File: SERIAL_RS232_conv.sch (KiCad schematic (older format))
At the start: 9 parts

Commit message: .bak ignore rule
Ignore bak files
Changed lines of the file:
@@
 $EndComp
 Wire Wire Line
-	2250 3550 2200 3550
-Wire Wire Line
-	2200 3550 2150 3550
+	2150 3550 2250 3550
 Wire Wire Line
 	1850 3550 1750 3550
 Wire Wire Line
-	1750 3350 1750 3550
+	1750 3350 1750 3750
 Wire Wire Line
-	1750 3550 1750 3750
-Wire Wire Line
-	1700 3750 1750 3750
-Wire Wire Line
-	1750 3750 2250 3750
+	1700 3750 2250 3750
 Wire Wire Line
 	2250 3950 2150 3950
@@
 	3650 3450 3700 3450
 Wire Wire Line
-	3700 3450 3700 3550
-Wire Wire Line
-	3700 3550 3700 3650
+	3700 3450 3700 3650
 Wire Wire Line
 	3700 3550 3750 3550
@@
 $EndComp
 Wire Wire Line
-	2200 3300 2200 3350
-Wire Wire Line
-	2200 3350 2200 3550
+	2200 3300 2200 3550
 Connection ~ 2200 3550
 Wire Wire Line

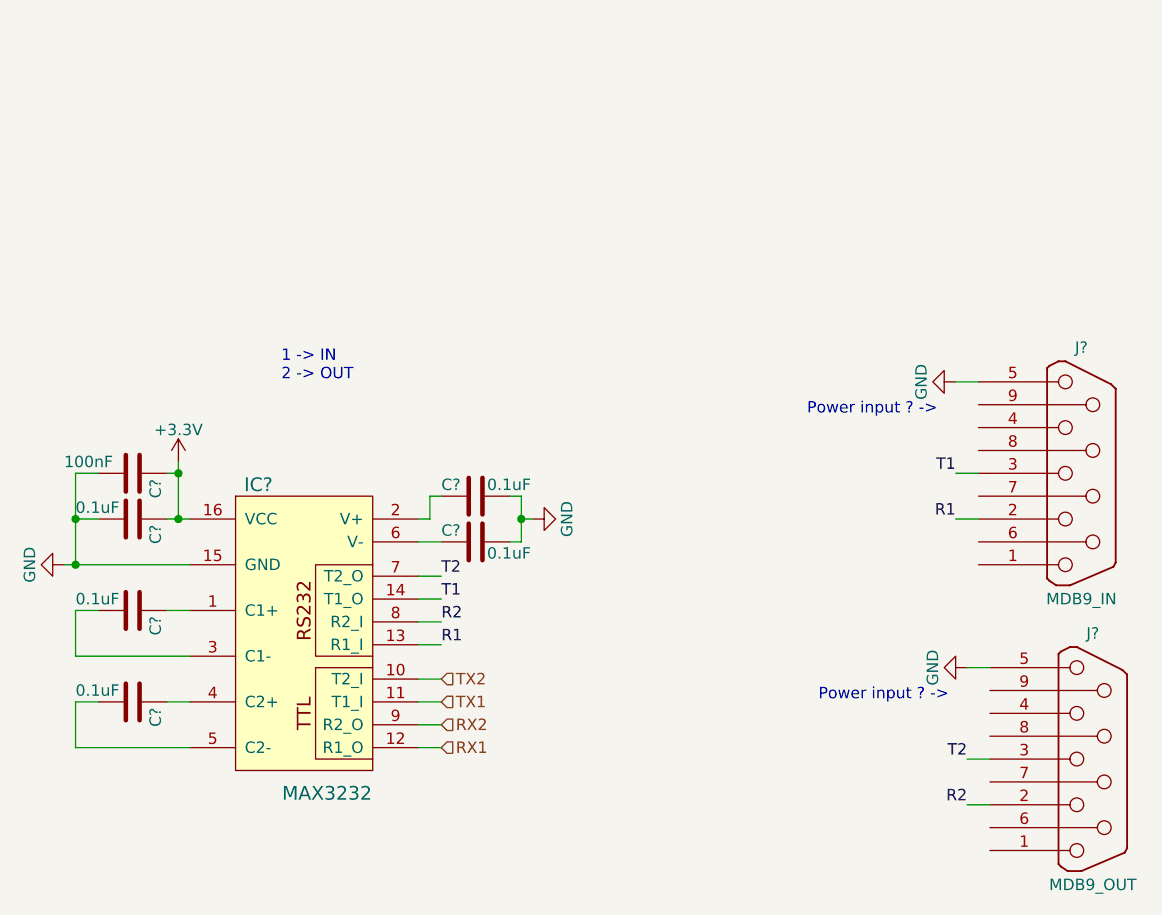
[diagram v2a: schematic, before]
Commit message: Schematic correction
Corrected the direction on some signals. Added a pin header for general development.
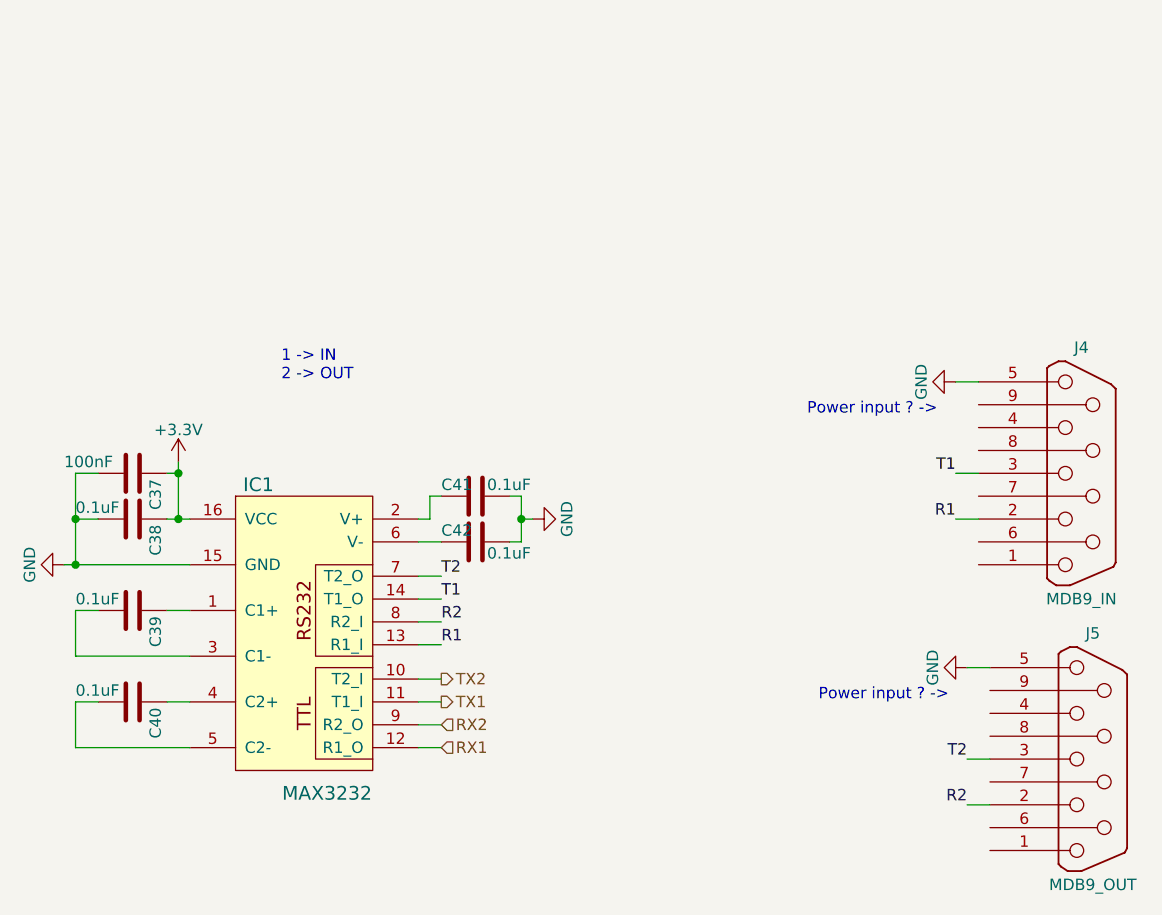
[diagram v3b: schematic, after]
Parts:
- C37, C38, C39, C40, C41, C42: renamed from C?; footprint (none) -> Capacitors_SMD:C_0603_HandSoldering
- gave numbers to parts that had none: 3
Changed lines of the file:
@@
 $EndDescr
 $Comp
-L MAX3232 IC?
+L MAX3232 IC1
 U 1 1 588F1DDD
 P 2750 3850
-F 0 "IC?" H 2550 4300 60  0000 C CNN
+F 0 "IC1" H 2550 4300 60  0000 C CNN
 F 1 "MAX3232" H 2850 2950 60  0000 C CNN
-F 2 "" H 2750 3850 60  0000 C CNN
+F 2 "" H 2750 3850 60  0001 C CNN
 F 3 "" H 2750 3850 60  0000 C CNN
 	1    2750 3850
@@
 $EndComp
 $Comp
-L DB9 J?
+L DB9 J4
 U 1 1 588F1EC2
 P 6150 3350
-F 0 "J?" H 6150 3900 50  0000 C CNN
+F 0 "J4" H 6150 3900 50  0000 C CNN
 F 1 "MDB9_IN" H 6150 2800 50  0000 C CNN
-F 2 "" H 6150 3350 50  0000 C CNN
+F 2 "" H 6150 3350 50  0001 C CNN
 F 3 "" H 6150 3350 50  0000 C CNN
 	1    6150 3350
@@
 $EndComp
 $Comp
-L DB9 J?
+L DB9 J5
 U 1 1 588F1F2B
 P 6200 4600
-F 0 "J?" H 6200 5150 50  0000 C CNN
+F 0 "J5" H 6200 5150 50  0000 C CNN
 F 1 "MDB9_OUT" H 6200 4050 50  0000 C CNN
-F 2 "" H 6200 4600 50  0000 C CNN
+F 2 "" H 6200 4600 50  0001 C CNN
 F 3 "" H 6200 4600 50  0000 C CNN
 	1    6200 4600
@@
 $EndComp
 $Comp
-L GND #PWR054
+L GND #PWR069
 U 1 1 588F1FE7
 P 5600 2950
-F 0 "#PWR054" H 5600 2700 50  0001 C CNN
+F 0 "#PWR069" H 5600 2700 50  0001 C CNN
 F 1 "GND" H 5600 2800 50  0000 C CNN
 F 2 "" H 5600 2950 50  0000 C CNN
@@
 $EndComp
 $Comp
-L GND #PWR055
+L GND #PWR070
 U 1 1 588F2002
 P 5650 4200
-F 0 "#PWR055" H 5650 3950 50  0001 C CNN
+F 0 "#PWR070" H 5650 3950 50  0001 C CNN
 F 1 "GND" H 5650 4050 50  0000 C CNN
 F 2 "" H 5650 4200 50  0000 C CNN
@@
 $EndComp
 $Comp
-L C C?
+L C C39
 U 1 1 588F207B
 P 2000 3950
-F 0 "C?" H 2025 4050 50  0000 L CNN
+F 0 "C39" H 2025 4050 50  0000 L CNN
 F 1 "0.1uF" V 1950 3700 50  0000 L CNN
-F 2 "" H 2038 3800 50  0000 C CNN
+F 2 "Capacitors_SMD:C_0603_HandSoldering" H 2038 3800 50  0001 C CNN
 F 3 "" H 2000 3950 50  0000 C CNN
 	1    2000 3950
@@
 $EndComp
 $Comp
-L C C?
+L C C40
 U 1 1 588F20EE
 P 2000 4350
-F 0 "C?" H 2025 4450 50  0000 L CNN
+F 0 "C40" H 2025 4450 50  0000 L CNN
 F 1 "0.1uF" V 1950 4100 50  0000 L CNN
-F 2 "" H 2038 4200 50  0000 C CNN
+F 2 "Capacitors_SMD:C_0603_HandSoldering" H 2038 4200 50  0001 C CNN
 F 3 "" H 2000 4350 50  0000 C CNN
 	1    2000 4350
@@
 $EndComp
 $Comp
-L C C?
+L C C38
 U 1 1 588F21DD
 P 2000 3550
-F 0 "C?" H 2025 3650 50  0000 L CNN
+F 0 "C38" H 2025 3650 50  0000 L CNN
 F 1 "0.1uF" V 1950 3300 50  0000 L CNN
-F 2 "" H 2038 3400 50  0000 C CNN
+F 2 "Capacitors_SMD:C_0603_HandSoldering" H 2038 3400 50  0001 C CNN
 F 3 "" H 2000 3550 50  0000 C CNN
 	1    2000 3550
@@
 	1750 4550 2250 4550
 $Comp
-L GND #PWR056
+L GND #PWR071
 U 1 1 588F251A
 P 3750 3550
-F 0 "#PWR056" H 3750 3300 50  0001 C CNN
+F 0 "#PWR071" H 3750 3300 50  0001 C CNN
 F 1 "GND" H 3750 3400 50  0000 C CNN
 F 2 "" H 3750 3550 50  0000 C CNN
@@
 Connection ~ 3700 3550
 $Comp
-L GND #PWR057
+L GND #PWR072
 U 1 1 588F266A
 P 1700 3750
-F 0 "#PWR057" H 1700 3500 50  0001 C CNN
+F 0 "#PWR072" H 1700 3500 50  0001 C CNN
 F 1 "GND" H 1700 3600 50  0000 C CNN
 F 2 "" H 1700 3750 50  0000 C CNN
@@
 Connection ~ 1750 3750
 $Comp
-L +3.3V #PWR058
+L +3.3V #PWR073
 U 1 1 588F26E1
 P 2200 3300
-F 0 "#PWR058" H 2200 3150 50  0001 C CNN
+F 0 "#PWR073" H 2200 3150 50  0001 C CNN
 F 1 "+3.3V" H 2200 3440 50  0000 C CNN
 F 2 "" H 2200 3300 50  0000 C CNN
@@
 $EndComp
 $Comp
-L C C?
+L C C37
 U 1 1 588F2970
 P 2000 3350
-F 0 "C?" H 2025 3450 50  0000 L CNN
+F 0 "C37" H 2025 3450 50  0000 L CNN
 F 1 "100nF" V 1950 3050 50  0000 L CNN
-F 2 "" H 2038 3200 50  0000 C CNN
+F 2 "Capacitors_SMD:C_0603_HandSoldering" H 2038 3200 50  0001 C CNN
 F 3 "" H 2000 3350 50  0000 C CNN
 	1    2000 3350
@@
 Connection ~ 1750 3550
 $Comp
-L C C?
+L C C41
 U 1 1 588F31D0
 P 3500 3450
-F 0 "C?" V 3450 3300 50  0000 L CNN
+F 0 "C41" V 3450 3300 50  0000 L CNN
 F 1 "0.1uF" V 3450 3500 50  0000 L CNN
-F 2 "" H 3538 3300 50  0000 C CNN
+F 2 "Capacitors_SMD:C_0603_HandSoldering" H 3538 3300 50  0001 C CNN
 F 3 "" H 3500 3450 50  0000 C CNN
 	1    3500 3450
@@
 $EndComp
 $Comp
-L C C?
+L C C42
 U 1 1 588F320C
 P 3500 3650
-F 0 "C?" V 3450 3500 50  0000 L CNN
+F 0 "C42" V 3450 3500 50  0000 L CNN
 F 1 "0.1uF" V 3550 3700 50  0000 L CNN
-F 2 "" H 3538 3500 50  0000 C CNN
+F 2 "Capacitors_SMD:C_0603_HandSoldering" H 3538 3500 50  0001 C CNN
 F 3 "" H 3500 3650 50  0000 C CNN
 	1    3500 3650
@@
 Wire Wire Line
 	5650 4200 5750 4200
-Text HLabel 3350 4350 2    50   Input ~ 0
+Text HLabel 3350 4350 2    50   Output ~ 0
 TX1
-Text HLabel 3350 4250 2    50   Input ~ 0
+Text HLabel 3350 4250 2    50   Output ~ 0
 TX2
 Text HLabel 3350 4450 2    50   Input ~ 0

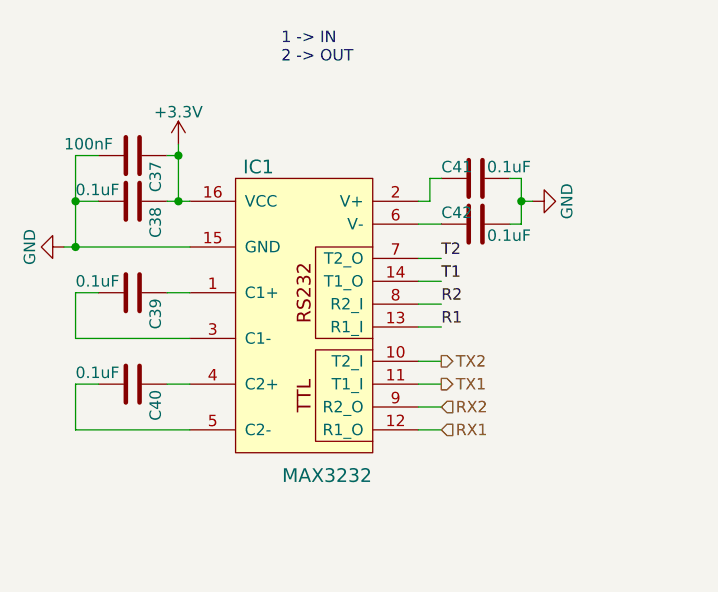
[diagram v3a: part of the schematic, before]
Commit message: Modified LAN9500A schematic.
Modified the schematic for the USB to Ethernet converter.
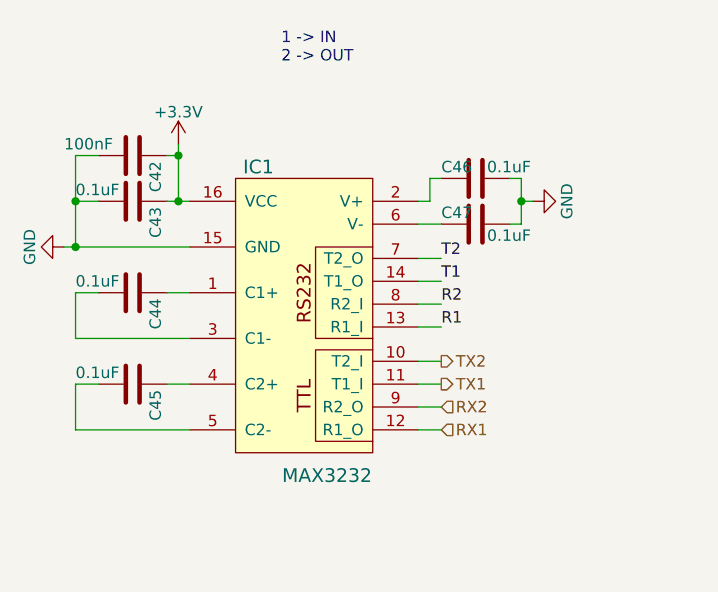
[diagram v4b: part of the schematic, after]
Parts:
- C42: renamed from C37; footprint Capacitors_SMD:C_0603_HandSoldering -> Capacitors_SMD:C_0805_HandSoldering
- C43: renamed from C38; footprint Capacitors_SMD:C_0603_HandSoldering -> Capacitors_SMD:C_0805_HandSoldering
- C44: renamed from C39; footprint Capacitors_SMD:C_0603_HandSoldering -> Capacitors_SMD:C_0805_HandSoldering
- C45: renamed from C40; footprint Capacitors_SMD:C_0603_HandSoldering -> Capacitors_SMD:C_0805_HandSoldering
- C46: renamed from C41; footprint Capacitors_SMD:C_0603_HandSoldering -> Capacitors_SMD:C_0805_HandSoldering
- C47: renamed from C42; footprint Capacitors_SMD:C_0603_HandSoldering -> Capacitors_SMD:C_0805_HandSoldering
- J4, J5: footprint (none) -> Connectors:DB9FC
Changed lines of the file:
@@
 F 0 "J4" H 6150 3900 50  0000 C CNN
 F 1 "MDB9_IN" H 6150 2800 50  0000 C CNN
-F 2 "" H 6150 3350 50  0001 C CNN
+F 2 "Connectors:DB9FC" H 6150 3350 50  0001 C CNN
 F 3 "" H 6150 3350 50  0000 C CNN
 	1    6150 3350
@@
 F 0 "J5" H 6200 5150 50  0000 C CNN
 F 1 "MDB9_OUT" H 6200 4050 50  0000 C CNN
-F 2 "" H 6200 4600 50  0001 C CNN
+F 2 "Connectors:DB9FC" H 6200 4600 50  0001 C CNN
 F 3 "" H 6200 4600 50  0000 C CNN
 	1    6200 4600
@@
 $EndComp
 $Comp
-L GND #PWR069
+L GND #PWR074
 U 1 1 588F1FE7
 P 5600 2950
-F 0 "#PWR069" H 5600 2700 50  0001 C CNN
+F 0 "#PWR074" H 5600 2700 50  0001 C CNN
 F 1 "GND" H 5600 2800 50  0000 C CNN
 F 2 "" H 5600 2950 50  0000 C CNN
@@
 $EndComp
 $Comp
-L GND #PWR070
+L GND #PWR075
 U 1 1 588F2002
 P 5650 4200
-F 0 "#PWR070" H 5650 3950 50  0001 C CNN
+F 0 "#PWR075" H 5650 3950 50  0001 C CNN
 F 1 "GND" H 5650 4050 50  0000 C CNN
 F 2 "" H 5650 4200 50  0000 C CNN
@@
 $EndComp
 $Comp
-L C C39
+L C C44
 U 1 1 588F207B
 P 2000 3950
-F 0 "C39" H 2025 4050 50  0000 L CNN
+F 0 "C44" H 2025 4050 50  0000 L CNN
 F 1 "0.1uF" V 1950 3700 50  0000 L CNN
-F 2 "Capacitors_SMD:C_0603_HandSoldering" H 2038 3800 50  0001 C CNN
+F 2 "Capacitors_SMD:C_0805_HandSoldering" H 2038 3800 50  0001 C CNN
 F 3 "" H 2000 3950 50  0000 C CNN
 	1    2000 3950
@@
 $EndComp
 $Comp
-L C C40
+L C C45
 U 1 1 588F20EE
 P 2000 4350
-F 0 "C40" H 2025 4450 50  0000 L CNN
+F 0 "C45" H 2025 4450 50  0000 L CNN
 F 1 "0.1uF" V 1950 4100 50  0000 L CNN
-F 2 "Capacitors_SMD:C_0603_HandSoldering" H 2038 4200 50  0001 C CNN
+F 2 "Capacitors_SMD:C_0805_HandSoldering" H 2038 4200 50  0001 C CNN
 F 3 "" H 2000 4350 50  0000 C CNN
 	1    2000 4350
@@
 $EndComp
 $Comp
-L C C38
+L C C43
 U 1 1 588F21DD
 P 2000 3550
-F 0 "C38" H 2025 3650 50  0000 L CNN
+F 0 "C43" H 2025 3650 50  0000 L CNN
 F 1 "0.1uF" V 1950 3300 50  0000 L CNN
-F 2 "Capacitors_SMD:C_0603_HandSoldering" H 2038 3400 50  0001 C CNN
+F 2 "Capacitors_SMD:C_0805_HandSoldering" H 2038 3400 50  0001 C CNN
 F 3 "" H 2000 3550 50  0000 C CNN
 	1    2000 3550
@@
 	1750 4550 2250 4550
 $Comp
-L GND #PWR071
+L GND #PWR076
 U 1 1 588F251A
 P 3750 3550
-F 0 "#PWR071" H 3750 3300 50  0001 C CNN
+F 0 "#PWR076" H 3750 3300 50  0001 C CNN
 F 1 "GND" H 3750 3400 50  0000 C CNN
 F 2 "" H 3750 3550 50  0000 C CNN
@@
 Connection ~ 3700 3550
 $Comp
-L GND #PWR072
+L GND #PWR077
 U 1 1 588F266A
 P 1700 3750
-F 0 "#PWR072" H 1700 3500 50  0001 C CNN
+F 0 "#PWR077" H 1700 3500 50  0001 C CNN
 F 1 "GND" H 1700 3600 50  0000 C CNN
 F 2 "" H 1700 3750 50  0000 C CNN
@@
 Connection ~ 1750 3750
 $Comp
-L +3.3V #PWR073
+L +3.3V #PWR078
 U 1 1 588F26E1
 P 2200 3300
-F 0 "#PWR073" H 2200 3150 50  0001 C CNN
+F 0 "#PWR078" H 2200 3150 50  0001 C CNN
 F 1 "+3.3V" H 2200 3440 50  0000 C CNN
 F 2 "" H 2200 3300 50  0000 C CNN
@@
 $EndComp
 $Comp
-L C C37
+L C C42
 U 1 1 588F2970
 P 2000 3350
-F 0 "C37" H 2025 3450 50  0000 L CNN
+F 0 "C42" H 2025 3450 50  0000 L CNN
 F 1 "100nF" V 1950 3050 50  0000 L CNN
-F 2 "Capacitors_SMD:C_0603_HandSoldering" H 2038 3200 50  0001 C CNN
+F 2 "Capacitors_SMD:C_0805_HandSoldering" H 2038 3200 50  0001 C CNN
 F 3 "" H 2000 3350 50  0000 C CNN
 	1    2000 3350
@@
 Connection ~ 1750 3550
 $Comp
-L C C41
+L C C46
 U 1 1 588F31D0
 P 3500 3450
-F 0 "C41" V 3450 3300 50  0000 L CNN
+F 0 "C46" V 3450 3300 50  0000 L CNN
 F 1 "0.1uF" V 3450 3500 50  0000 L CNN
-F 2 "Capacitors_SMD:C_0603_HandSoldering" H 3538 3300 50  0001 C CNN
+F 2 "Capacitors_SMD:C_0805_HandSoldering" H 3538 3300 50  0001 C CNN
 F 3 "" H 3500 3450 50  0000 C CNN
 	1    3500 3450
@@
 $EndComp
 $Comp
-L C C42
+L C C47
 U 1 1 588F320C
 P 3500 3650
-F 0 "C42" V 3450 3500 50  0000 L CNN
+F 0 "C47" V 3450 3500 50  0000 L CNN
 F 1 "0.1uF" V 3550 3700 50  0000 L CNN
-F 2 "Capacitors_SMD:C_0603_HandSoldering" H 3538 3500 50  0001 C CNN
+F 2 "Capacitors_SMD:C_0805_HandSoldering" H 3538 3500 50  0001 C CNN
 F 3 "" H 3500 3650 50  0000 C CNN
 	1    3500 3650

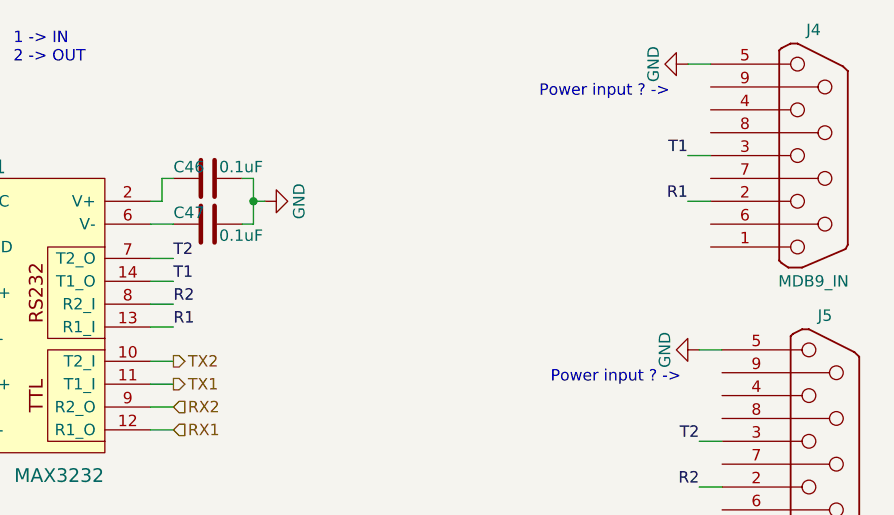
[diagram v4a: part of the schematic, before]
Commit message: Schematic changes. PCB in process of making.
Removed LAN9500A Jtag. Removed Aria G25 pinout. Removed USB connectors. Added rezistors to USB/ETH/ySD shields.
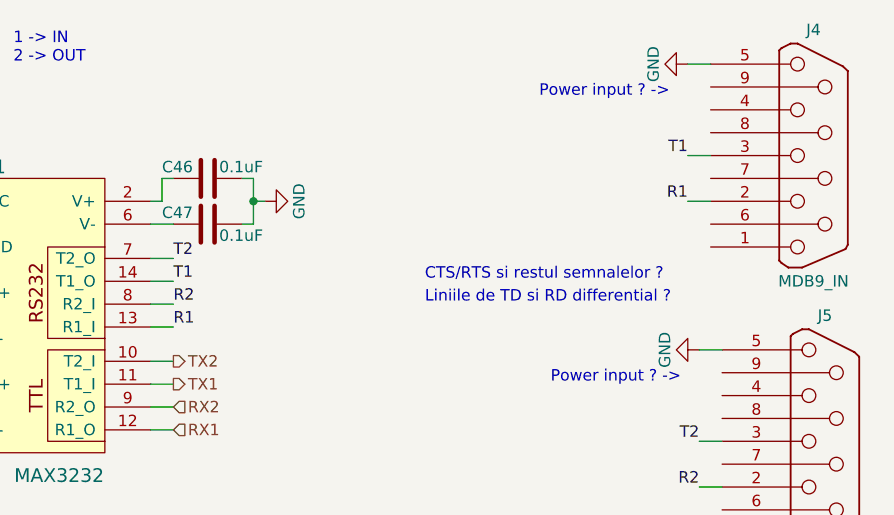
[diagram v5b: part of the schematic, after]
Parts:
- IC1: footprint (none) -> SMD_Packages:SO-16-L
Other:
- note added: "CTS/RTS si restul semnalelor ?"
- note added: "Liniile de TD si RD differential ?"
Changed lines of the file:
@@
 F 0 "IC1" H 2550 4300 60  0000 C CNN
 F 1 "MAX3232" H 2850 2950 60  0000 C CNN
-F 2 "" H 2750 3850 60  0001 C CNN
+F 2 "SMD_Packages:SO-16-L" H 2750 3850 60  0001 C CNN
 F 3 "" H 2750 3850 60  0000 C CNN
 	1    2750 3850
@@
 $EndComp
 $Comp
-L GND #PWR074
+L GND #PWR064
 U 1 1 588F1FE7
 P 5600 2950
-F 0 "#PWR074" H 5600 2700 50  0001 C CNN
+F 0 "#PWR064" H 5600 2700 50  0001 C CNN
 F 1 "GND" H 5600 2800 50  0000 C CNN
 F 2 "" H 5600 2950 50  0000 C CNN
@@
 $EndComp
 $Comp
-L GND #PWR075
+L GND #PWR065
 U 1 1 588F2002
 P 5650 4200
-F 0 "#PWR075" H 5650 3950 50  0001 C CNN
+F 0 "#PWR065" H 5650 3950 50  0001 C CNN
 F 1 "GND" H 5650 4050 50  0000 C CNN
 F 2 "" H 5650 4200 50  0000 C CNN
@@
 	1750 4550 2250 4550
 $Comp
-L GND #PWR076
+L GND #PWR066
 U 1 1 588F251A
 P 3750 3550
-F 0 "#PWR076" H 3750 3300 50  0001 C CNN
+F 0 "#PWR066" H 3750 3300 50  0001 C CNN
 F 1 "GND" H 3750 3400 50  0000 C CNN
 F 2 "" H 3750 3550 50  0000 C CNN
@@
 Connection ~ 3700 3550
 $Comp
-L GND #PWR077
+L GND #PWR067
 U 1 1 588F266A
 P 1700 3750
-F 0 "#PWR077" H 1700 3500 50  0001 C CNN
+F 0 "#PWR067" H 1700 3500 50  0001 C CNN
 F 1 "GND" H 1700 3600 50  0000 C CNN
 F 2 "" H 1700 3750 50  0000 C CNN
@@
 Connection ~ 1750 3750
 $Comp
-L +3.3V #PWR078
+L +3.3V #PWR068
 U 1 1 588F26E1
 P 2200 3300
-F 0 "#PWR078" H 2200 3150 50  0001 C CNN
+F 0 "#PWR068" H 2200 3150 50  0001 C CNN
 F 1 "+3.3V" H 2200 3440 50  0000 C CNN
 F 2 "" H 2200 3300 50  0000 C CNN
@@
 U 1 1 588F31D0
 P 3500 3450
-F 0 "C46" V 3450 3300 50  0000 L CNN
+F 0 "C46" V 3450 3250 50  0000 L CNN
 F 1 "0.1uF" V 3450 3500 50  0000 L CNN
 F 2 "Capacitors_SMD:C_0805_HandSoldering" H 3538 3300 50  0001 C CNN
@@
 U 1 1 588F320C
 P 3500 3650
-F 0 "C47" V 3450 3500 50  0000 L CNN
+F 0 "C47" V 3450 3450 50  0000 L CNN
 F 1 "0.1uF" V 3550 3700 50  0000 L CNN
 F 2 "Capacitors_SMD:C_0805_HandSoldering" H 3538 3500 50  0001 C CNN
@@
 Text Notes 5000 4350 0    50   ~ 0
 Power input ? ->
+Text Notes 4450 3900 0    50   ~ 0
+CTS/RTS si restul semnalelor ?
+Text Notes 4450 4000 0    50   ~ 0
+Liniile de TD si RD differential ?
 $EndSCHEMATC

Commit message: Modified buck circuit on board.
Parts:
- C42, C43, C44, C45, C46, C47: footprint Capacitors_SMD:C_0805_HandSoldering -> Capacitors_SMD:C_0603_HandSoldering
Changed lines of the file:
@@
 F 0 "C44" H 2025 4050 50  0000 L CNN
 F 1 "0.1uF" V 1950 3700 50  0000 L CNN
-F 2 "Capacitors_SMD:C_0805_HandSoldering" H 2038 3800 50  0001 C CNN
+F 2 "Capacitors_SMD:C_0603_HandSoldering" H 2038 3800 50  0001 C CNN
 F 3 "" H 2000 3950 50  0000 C CNN
 	1    2000 3950
@@
 F 0 "C45" H 2025 4450 50  0000 L CNN
 F 1 "0.1uF" V 1950 4100 50  0000 L CNN
-F 2 "Capacitors_SMD:C_0805_HandSoldering" H 2038 4200 50  0001 C CNN
+F 2 "Capacitors_SMD:C_0603_HandSoldering" H 2038 4200 50  0001 C CNN
 F 3 "" H 2000 4350 50  0000 C CNN
 	1    2000 4350
@@
 F 0 "C43" H 2025 3650 50  0000 L CNN
 F 1 "0.1uF" V 1950 3300 50  0000 L CNN
-F 2 "Capacitors_SMD:C_0805_HandSoldering" H 2038 3400 50  0001 C CNN
+F 2 "Capacitors_SMD:C_0603_HandSoldering" H 2038 3400 50  0001 C CNN
 F 3 "" H 2000 3550 50  0000 C CNN
 	1    2000 3550
@@
 F 0 "C42" H 2025 3450 50  0000 L CNN
 F 1 "100nF" V 1950 3050 50  0000 L CNN
-F 2 "Capacitors_SMD:C_0805_HandSoldering" H 2038 3200 50  0001 C CNN
+F 2 "Capacitors_SMD:C_0603_HandSoldering" H 2038 3200 50  0001 C CNN
 F 3 "" H 2000 3350 50  0000 C CNN
 	1    2000 3350
@@
 F 0 "C46" V 3450 3250 50  0000 L CNN
 F 1 "0.1uF" V 3450 3500 50  0000 L CNN
-F 2 "Capacitors_SMD:C_0805_HandSoldering" H 3538 3300 50  0001 C CNN
+F 2 "Capacitors_SMD:C_0603_HandSoldering" H 3538 3300 50  0001 C CNN
 F 3 "" H 3500 3450 50  0000 C CNN
 	1    3500 3450
@@
 F 0 "C47" V 3450 3450 50  0000 L CNN
 F 1 "0.1uF" V 3550 3700 50  0000 L CNN
-F 2 "Capacitors_SMD:C_0805_HandSoldering" H 3538 3500 50  0001 C CNN
+F 2 "Capacitors_SMD:C_0603_HandSoldering" H 3538 3500 50  0001 C CNN
 F 3 "" H 3500 3650 50  0000 C CNN
 	1    3500 3650
